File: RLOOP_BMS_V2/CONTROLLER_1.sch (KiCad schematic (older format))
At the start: 21 parts

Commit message: Bug Fixes
A few fixes and cleanup to make the ERC happy.
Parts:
- removed C? (x3): 100 nF / 50V/ 10% / SMD 0603, symbol C
- removed C?: 100n / 50V / 10% / SMD 0603, symbol C
- removed C? (x2): 100nF / 50V / 10% / SMD 0603, symbol C
- removed C? (x2): 10uF / 25V / 20% / SMD 1206, symbol C
- removed IC?: ATA6870N-PLQW-1, symbol ATA6870N-PLQW-1
- removed R?: 121K / 0.1W / 1% / SMD 0603, symbol R
- removed R? (x2): 10K / .1 W / 1% / SMD 0603, symbol R
- removed R?: 10, symbol R
- removed R?: 100k, symbol R
- removed TH? (x2): NTCS0603E3103JLT, symbol Thermistor_NTC
- added C16, C17: 10uF / 25V / 20% / SMD 1206, symbol C
- added C18, C20: 100nF / 50V / 10% / SMD 0603, symbol C
- added C19: 100n / 50V / 10% / SMD 0603, symbol C
- added C21, C22, C24: 100 nF / 50V/ 10% / SMD 0603, symbol C
- added IC4: ATA6870N-PLQW-1, symbol ATA6870N-PLQW-1
- added R12: 10, symbol R
- added R13: 121K / 0.1W / 1% / SMD 0603, symbol R
- added R14, R15: 10K / .1 W / 1% / SMD 0603, symbol R
- added TH3, TH4: NTCS0603E3103JLT, symbol Thermistor_NTC
- gave numbers to parts that had none: 5
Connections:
- net labels added: VDDHVP
- net labels removed: Thermal_Pad_3, ~PD_OUT
- wire segments 89 -> 86
- no-connect marks 0 -> 3
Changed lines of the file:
@@
 VDDHVM
 $Comp
-L ATA6870N-PLQW-1 IC?
-U 1 1 591D6F2A
+L ATA6870N-PLQW-1 IC4
+U 1 1 5917E38B
 P 5600 3400
-F 0 "IC?" H 6300 5200 60  0000 C CNN
+F 0 "IC4" H 6300 5200 60  0000 C CNN
 F 1 "ATA6870N-PLQW-1" H 6650 5100 60  0000 C CNN
 F 2 "" H 5550 3400 60  0001 C CNN
@@
 	-1   0    0    -1
 $EndComp
-Text HLabel 4100 2300 0    60   Output ~ 0
-~PD_OUT
 Text HLabel 2250 6900 0    60   Input ~ 0
 VDDHV
@@
 GND_1
 $Comp
-L C C?
-U 1 1 59101A84
+L C C21
+U 1 1 5917E364
 P 8350 1950
-F 0 "C?" H 8100 1950 50  0000 L CNN
+F 0 "C21" H 8100 1950 50  0000 L CNN
 F 1 "100 nF / 50V/ 10% / SMD 0603" H 8500 1950 50  0000 L CNN
 F 2 "" H 8388 1800 50  0001 C CNN
@@
 $EndComp
 $Comp
-L C C?
-U 1 1 59101A9B
+L C C22
+U 1 1 5917E366
 P 8350 2250
-F 0 "C?" H 8100 2250 50  0000 L CNN
+F 0 "C22" H 8100 2250 50  0000 L CNN
 F 1 "100 nF / 50V/ 10% / SMD 0603" H 8500 2250 50  0000 L CNN
 F 2 "" H 8388 2100 50  0001 C CNN
@@
 $EndComp
 $Comp
-L C C?
+L C C23
 U 1 1 59101AC2
 P 8350 2550
-F 0 "C?" H 8100 2550 50  0000 L CNN
+F 0 "C23" H 8100 2550 50  0000 L CNN
 F 1 "100 nF / 50V/ 10% / SMD 0603" H 8500 2550 50  0000 L CNN
 F 2 "" H 8388 2400 50  0001 C CNN
@@
 $EndComp
 $Comp
-L C C?
-U 1 1 59101ADD
+L C C24
+U 1 1 5917E36A
 P 8350 2850
-F 0 "C?" H 8100 2850 50  0000 L CNN
+F 0 "C24" H 8100 2850 50  0000 L CNN
 F 1 "100 nF / 50V/ 10% / SMD 0603" H 8500 2850 50  0000 L CNN
 F 2 "" H 8388 2700 50  0001 C CNN
@@
 $EndComp
 $Comp
-L C C?
+L C C25
 U 1 1 59101B02
 P 8350 3150
-F 0 "C?" H 8100 3150 50  0000 L CNN
+F 0 "C25" H 8100 3150 50  0000 L CNN
 F 1 "100 nF / 50V/ 10% / SMD 0603" H 8500 3150 50  0000 L CNN
 F 2 "" H 8388 3000 50  0001 C CNN
@@
 $EndComp
 $Comp
-L C C?
+L C C26
 U 1 1 59101B2D
 P 8350 3450
-F 0 "C?" H 8100 3450 50  0000 L CNN
+F 0 "C26" H 8100 3450 50  0000 L CNN
 F 1 "100 nF / 50V/ 10% / SMD 0603" H 8500 3450 50  0000 L CNN
 F 2 "" H 8388 3300 50  0001 C CNN
@@
 $EndComp
 $Comp
-L R R?
-U 1 1 59102664
+L R R13
+U 1 1 5917E371
 P 6900 4350
-F 0 "R?" V 6980 4350 50  0000 C CNN
+F 0 "R13" V 6980 4350 50  0000 C CNN
 F 1 "121K / 0.1W / 1% / SMD 0603" V 7050 4850 50  0000 C CNN
 F 2 "" V 6830 4350 50  0001 C CNN
@@
 GND_1
 $Comp
-L R R?
-U 1 1 591040ED
+L R R15
+U 1 1 5917E372
 P 9950 4050
-F 0 "R?" V 10030 4050 50  0000 C CNN
+F 0 "R15" V 10030 4050 50  0000 C CNN
 F 1 "10K / .1 W / 1% / SMD 0603" H 9300 4050 50  0000 C CNN
 F 2 "" V 9880 4050 50  0001 C CNN
@@
 $EndComp
 $Comp
-L Thermistor_NTC TH?
-U 1 1 59104176
+L Thermistor_NTC TH4
+U 1 1 5917E374
 P 9950 4550
-F 0 "TH?" V 9775 4550 50  0000 C CNN
+F 0 "TH4" V 9775 4550 50  0000 C CNN
 F 1 "NTCS0603E3103JLT" H 10450 4550 50  0000 C CNN
 F 2 "" H 9950 4600 50  0001 C CNN
@@
 $EndComp
 $Comp
-L Thermistor_NTC TH?
-U 1 1 5910419D
+L Thermistor_NTC TH3
+U 1 1 5917E377
 P 9000 4550
-F 0 "TH?" V 8825 4550 50  0000 C CNN
+F 0 "TH3" V 8825 4550 50  0000 C CNN
 F 1 "NTCS0603E3103JLT" H 9000 4350 50  0000 C CNN
 F 2 "" H 9000 4600 50  0001 C CNN
@@
 $EndComp
 $Comp
-L R R?
-U 1 1 591041CA
+L R R14
+U 1 1 5917E378
 P 9000 4050
-F 0 "R?" V 9080 4050 50  0000 C CNN
+F 0 "R14" V 9080 4050 50  0000 C CNN
 F 1 "10K / .1 W / 1% / SMD 0603" H 9200 4200 50  0000 C CNN
 F 2 "" V 8930 4050 50  0001 C CNN
@@
 GND_1
 $Comp
-L C C?
+L C C28
 U 1 1 59105042
 P 9550 4550
-F 0 "C?" H 9575 4650 50  0000 L CNN
+F 0 "C28" H 9575 4650 50  0000 L CNN
 F 1 "100n" H 9250 4550 50  0000 L CNN
 F 2 "" H 9588 4400 50  0001 C CNN
@@
 $EndComp
 $Comp
-L C C?
+L C C27
 U 1 1 591051E7
 P 8450 4550
-F 0 "C?" H 8475 4650 50  0000 L CNN
+F 0 "C27" H 8475 4650 50  0000 L CNN
 F 1 "100n" H 8200 4450 50  0000 L CNN
 F 2 "" H 8488 4400 50  0001 C CNN
@@
 $EndComp
 $Comp
-L R R?
-U 1 1 5910D275
+L R R12
+U 1 1 5917E381
 P 2650 6900
-F 0 "R?" V 2730 6900 50  0000 C CNN
+F 0 "R12" V 2730 6900 50  0000 C CNN
 F 1 "10" V 2650 6900 50  0000 C CNN
 F 2 "" V 2580 6900 50  0001 C CNN
@@
 $EndComp
 $Comp
-L C C?
-U 1 1 5910D5BF
+L C C20
+U 1 1 5917E382
 P 6750 2000
-F 0 "C?" H 6775 2100 50  0000 L CNN
+F 0 "C20" H 6775 2100 50  0000 L CNN
 F 1 "100nF / 50V / 10% / SMD 0603" H 5400 2150 50  0000 L CNN
 F 2 "" H 6788 1850 50  0001 C CNN
@@
 $EndComp
 $Comp
-L C C?
-U 1 1 5910D5FC
+L C C17
+U 1 1 5917E385
 P 3200 7150
-F 0 "C?" H 3225 7250 50  0000 L CNN
+F 0 "C17" H 3225 7250 50  0000 L CNN
 F 1 "10uF / 25V / 20% / SMD 1206" H 1750 7150 50  0000 L CNN
 F 2 "" H 3238 7000 50  0001 C CNN
@@
 $EndComp
 $Comp
-L R R?
-U 1 1 591108C7
-P 4200 4850
-F 0 "R?" V 4100 4850 50  0000 C CNN
-F 1 "100k" V 4200 4850 50  0000 C CNN
-F 2 "" V 4130 4850 50  0001 C CNN
-F 3 "" H 4200 4850 50  0001 C CNN
-	1    4200 4850
-	0    1    1    0
-$EndComp
-$Comp
-L C C?
-U 1 1 5910B934
+L C C19
+U 1 1 5917E37E
 P 5450 1700
-F 0 "C?" H 5475 1800 50  0000 L CNN
+F 0 "C19" H 5475 1800 50  0000 L CNN
 F 1 "100n / 50V / 10% / SMD 0603" H 5250 1900 50  0000 L CNN
 F 2 "" H 5488 1550 50  0001 C CNN
@@
 Text GLabel 6850 2200 2    60   Input ~ 0
 VDDHV_1
-Text GLabel 4100 2550 0    60   Input ~ 0
-VDDHV_1
-Text Label 5200 6000 1    60   ~ 0
-Thermal_Pad_3
 Text GLabel 6750 1750 1    60   Input ~ 0
 GND_1
 $Comp
-L C C?
-U 1 1 59119745
+L C C18
+U 1 1 5917E386
 P 3250 2800
-F 0 "C?" H 3275 2900 50  0000 L CNN
+F 0 "C18" H 3275 2900 50  0000 L CNN
 F 1 "100nF / 50V / 10% / SMD 0603" H 3275 2700 50  0000 L CNN
 F 2 "" H 3288 2650 50  0001 C CNN
@@
 Wire Wire Line
 	4100 2200 4450 2200
-Wire Wire Line
-	4450 2300 4100 2300
 Wire Wire Line
 	4100 3850 4450 3850
@@
 Connection ~ 5850 5450
 Wire Wire Line
-	4450 4850 4350 4850
-Wire Wire Line
-	3900 4850 4050 4850
-Wire Wire Line
-	3550 4950 4450 4950
-Wire Wire Line
 	4300 1850 5650 1850
 Connection ~ 5450 1850
@@
 	4100 2550 4450 2550
 Wire Wire Line
-	5250 5300 5250 6000
-Wire Wire Line
 	6650 3800 9950 3800
 Wire Wire Line
@@
 Connection ~ 9000 5100
 Wire Wire Line
-	5250 6000 5200 6000
-Wire Wire Line
 	6750 2150 6750 2200
 Connection ~ 6750 2200
@@
 Connection ~ 3250 2650
 $Comp
-L C C?
-U 1 1 5911BED4
+L C C16
+U 1 1 5917E388
 P 2700 2800
-F 0 "C?" H 2725 2900 50  0000 L CNN
+F 0 "C16" H 2725 2900 50  0000 L CNN
 F 1 "10uF / 25V / 20% / SMD 1206" H 1300 2800 50  0000 L CNN
 F 2 "" H 2738 2650 50  0001 C CNN
@@
 Wire Wire Line
 	4450 3650 4100 3650
-Text GLabel 3550 4950 0    60   Input ~ 0
-GND_1
-Wire Wire Line
-	3900 4750 3900 4950
-Connection ~ 3900 4950
-Wire Wire Line
-	4450 4750 3900 4750
-Connection ~ 3900 4850
 Wire Wire Line
 	4300 4550 4450 4550
 Connection ~ 4300 2850
+Text HLabel 4100 2550 0    60   Input ~ 0
+VDDHVP
+NoConn ~ 4450 4950
+NoConn ~ 4450 4850
+NoConn ~ 4450 4750
+Text GLabel 4100 2300 0    60   Input ~ 0
+GND_1
+Wire Wire Line
+	4100 2300 4450 2300
+Text GLabel 12250 2950 0    60   Input ~ 0
+GND_1
+Text GLabel 12250 3200 0    60   Input ~ 0
+VDDHV_1
+$Comp
+L PWR_FLAG #FLG03
+U 1 1 591903A2
+P 12500 2650
+F 0 "#FLG03" H 12500 2725 50  0001 C CNN
+F 1 "PWR_FLAG" H 12500 2800 50  0000 C CNN
+F 2 "" H 12500 2650 50  0001 C CNN
+F 3 "" H 12500 2650 50  0001 C CNN
+	1    12500 2650
+	1    0    0    -1
+$EndComp
+$Comp
+L PWR_FLAG #FLG04
+U 1 1 591903DE
+P 13000 2650
+F 0 "#FLG04" H 13000 2725 50  0001 C CNN
+F 1 "PWR_FLAG" H 13000 2800 50  0000 C CNN
+F 2 "" H 13000 2650 50  0001 C CNN
+F 3 "" H 13000 2650 50  0001 C CNN
+	1    13000 2650
+	1    0    0    -1
+$EndComp
+Wire Wire Line
+	12500 2650 12500 2950
+Wire Wire Line
+	12500 2950 12250 2950
+Wire Wire Line
+	12250 3200 13000 3200
+Wire Wire Line
+	13000 3200 13000 2650
 $EndSCHEMATC

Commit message: Footprint work
starting to assign footprints to parts
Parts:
- C16, C17: footprint (none) -> Capacitors_SMD:C_1206
- C18, C19, C20, C21, C22, C23, C24, C25, C26, C27, C28: footprint (none) -> Capacitors_SMD:C_0603
- R12, R13, R14, R15: footprint (none) -> Resistors_SMD:R_0603
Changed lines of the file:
@@
 F 0 "C21" H 8100 1950 50  0000 L CNN
 F 1 "100 nF / 50V/ 10% / SMD 0603" H 8500 1950 50  0000 L CNN
-F 2 "" H 8388 1800 50  0001 C CNN
+F 2 "Capacitors_SMD:C_0603" H 8388 1800 50  0001 C CNN
 F 3 "" H 8350 1950 50  0001 C CNN
 	1    8350 1950
@@
 F 0 "C22" H 8100 2250 50  0000 L CNN
 F 1 "100 nF / 50V/ 10% / SMD 0603" H 8500 2250 50  0000 L CNN
-F 2 "" H 8388 2100 50  0001 C CNN
+F 2 "Capacitors_SMD:C_0603" H 8388 2100 50  0001 C CNN
 F 3 "" H 8350 2250 50  0001 C CNN
 	1    8350 2250
@@
 F 0 "C23" H 8100 2550 50  0000 L CNN
 F 1 "100 nF / 50V/ 10% / SMD 0603" H 8500 2550 50  0000 L CNN
-F 2 "" H 8388 2400 50  0001 C CNN
+F 2 "Capacitors_SMD:C_0603" H 8388 2400 50  0001 C CNN
 F 3 "" H 8350 2550 50  0001 C CNN
 	1    8350 2550
@@
 F 0 "C24" H 8100 2850 50  0000 L CNN
 F 1 "100 nF / 50V/ 10% / SMD 0603" H 8500 2850 50  0000 L CNN
-F 2 "" H 8388 2700 50  0001 C CNN
+F 2 "Capacitors_SMD:C_0603" H 8388 2700 50  0001 C CNN
 F 3 "" H 8350 2850 50  0001 C CNN
 	1    8350 2850
@@
 F 0 "C25" H 8100 3150 50  0000 L CNN
 F 1 "100 nF / 50V/ 10% / SMD 0603" H 8500 3150 50  0000 L CNN
-F 2 "" H 8388 3000 50  0001 C CNN
+F 2 "Capacitors_SMD:C_0603" H 8388 3000 50  0001 C CNN
 F 3 "" H 8350 3150 50  0001 C CNN
 	1    8350 3150
@@
 F 0 "C26" H 8100 3450 50  0000 L CNN
 F 1 "100 nF / 50V/ 10% / SMD 0603" H 8500 3450 50  0000 L CNN
-F 2 "" H 8388 3300 50  0001 C CNN
+F 2 "Capacitors_SMD:C_0603" H 8388 3300 50  0001 C CNN
 F 3 "" H 8350 3450 50  0001 C CNN
 	1    8350 3450
@@
 F 0 "R13" V 6980 4350 50  0000 C CNN
 F 1 "121K / 0.1W / 1% / SMD 0603" V 7050 4850 50  0000 C CNN
-F 2 "" V 6830 4350 50  0001 C CNN
+F 2 "Resistors_SMD:R_0603" V 6830 4350 50  0001 C CNN
 F 3 "" H 6900 4350 50  0001 C CNN
 	1    6900 4350
@@
 F 0 "R15" V 10030 4050 50  0000 C CNN
 F 1 "10K / .1 W / 1% / SMD 0603" H 9300 4050 50  0000 C CNN
-F 2 "" V 9880 4050 50  0001 C CNN
+F 2 "Resistors_SMD:R_0603" V 9880 4050 50  0001 C CNN
 F 3 "" H 9950 4050 50  0001 C CNN
 	1    9950 4050
@@
 F 0 "R14" V 9080 4050 50  0000 C CNN
 F 1 "10K / .1 W / 1% / SMD 0603" H 9200 4200 50  0000 C CNN
-F 2 "" V 8930 4050 50  0001 C CNN
+F 2 "Resistors_SMD:R_0603" V 8930 4050 50  0001 C CNN
 F 3 "" H 9000 4050 50  0001 C CNN
 	1    9000 4050
@@
 F 0 "C28" H 9575 4650 50  0000 L CNN
 F 1 "100n" H 9250 4550 50  0000 L CNN
-F 2 "" H 9588 4400 50  0001 C CNN
+F 2 "Capacitors_SMD:C_0603" H 9588 4400 50  0001 C CNN
 F 3 "" H 9550 4550 50  0001 C CNN
 	1    9550 4550
@@
 F 0 "C27" H 8475 4650 50  0000 L CNN
 F 1 "100n" H 8200 4450 50  0000 L CNN
-F 2 "" H 8488 4400 50  0001 C CNN
+F 2 "Capacitors_SMD:C_0603" H 8488 4400 50  0001 C CNN
 F 3 "" H 8450 4550 50  0001 C CNN
 	1    8450 4550
@@
 F 0 "R12" V 2730 6900 50  0000 C CNN
 F 1 "10" V 2650 6900 50  0000 C CNN
-F 2 "" V 2580 6900 50  0001 C CNN
+F 2 "Resistors_SMD:R_0603" V 2580 6900 50  0001 C CNN
 F 3 "" H 2650 6900 50  0001 C CNN
 	1    2650 6900
@@
 F 0 "C20" H 6775 2100 50  0000 L CNN
 F 1 "100nF / 50V / 10% / SMD 0603" H 5400 2150 50  0000 L CNN
-F 2 "" H 6788 1850 50  0001 C CNN
+F 2 "Capacitors_SMD:C_0603" H 6788 1850 50  0001 C CNN
 F 3 "" H 6750 2000 50  0001 C CNN
 	1    6750 2000
@@
 F 0 "C17" H 3225 7250 50  0000 L CNN
 F 1 "10uF / 25V / 20% / SMD 1206" H 1750 7150 50  0000 L CNN
-F 2 "" H 3238 7000 50  0001 C CNN
+F 2 "Capacitors_SMD:C_1206" H 3238 7000 50  0001 C CNN
 F 3 "" H 3200 7150 50  0001 C CNN
 	1    3200 7150
@@
 F 0 "C19" H 5475 1800 50  0000 L CNN
 F 1 "100n / 50V / 10% / SMD 0603" H 5250 1900 50  0000 L CNN
-F 2 "" H 5488 1550 50  0001 C CNN
+F 2 "Capacitors_SMD:C_0603" H 5488 1550 50  0001 C CNN
 F 3 "" H 5450 1700 50  0001 C CNN
 	1    5450 1700
@@
 F 0 "C18" H 3275 2900 50  0000 L CNN
 F 1 "100nF / 50V / 10% / SMD 0603" H 3275 2700 50  0000 L CNN
-F 2 "" H 3288 2650 50  0001 C CNN
+F 2 "Capacitors_SMD:C_0603" H 3288 2650 50  0001 C CNN
 F 3 "" H 3250 2800 50  0001 C CNN
 	1    3250 2800
@@
 F 0 "C16" H 2725 2900 50  0000 L CNN
 F 1 "10uF / 25V / 20% / SMD 1206" H 1300 2800 50  0000 L CNN
-F 2 "" H 2738 2650 50  0001 C CNN
+F 2 "Capacitors_SMD:C_1206" H 2738 2650 50  0001 C CNN
 F 3 "" H 2700 2800 50  0001 C CNN
 	1    2700 2800

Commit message: footprint and layout work WIP
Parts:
- IC4: footprint (none) -> rLoop_Footprints:ATA6870-QFN48
- TH3, TH4: footprint (none) -> Resistors_SMD:R_0603
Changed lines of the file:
@@
 F 0 "IC4" H 6300 5200 60  0000 C CNN
 F 1 "ATA6870N-PLQW-1" H 6650 5100 60  0000 C CNN
-F 2 "" H 5550 3400 60  0001 C CNN
+F 2 "rLoop_Footprints:ATA6870-QFN48" H 5550 3400 60  0001 C CNN
 F 3 "" H 5550 3400 60  0001 C CNN
 	1    5600 3400
@@
 F 0 "TH4" V 9775 4550 50  0000 C CNN
 F 1 "NTCS0603E3103JLT" H 10450 4550 50  0000 C CNN
-F 2 "" H 9950 4600 50  0001 C CNN
+F 2 "Resistors_SMD:R_0603" H 9950 4600 50  0001 C CNN
 F 3 "" H 9950 4600 50  0001 C CNN
 	1    9950 4550
@@
 F 0 "TH3" V 8825 4550 50  0000 C CNN
 F 1 "NTCS0603E3103JLT" H 9000 4350 50  0000 C CNN
-F 2 "" H 9000 4600 50  0001 C CNN
+F 2 "Resistors_SMD:R_0603" H 9000 4600 50  0001 C CNN
 F 3 "" H 9000 4600 50  0001 C CNN
 	1    9000 4550

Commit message: WIP
See if it's even possible
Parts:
- removed C16, C17: 10uF / 25V / 20% / SMD 1206, Capacitors_SMD:C_1206, symbol C
- removed C18, C20: 100nF / 50V / 10% / SMD 0603, Capacitors_SMD:C_0603, symbol C
- removed C19: 100n / 50V / 10% / SMD 0603, Capacitors_SMD:C_0603, symbol C
- removed C27, C28: 100n, Capacitors_SMD:C_0603, symbol C
- removed IC4: ATA6870N-PLQW-1, rLoop_Footprints:ATA6870-QFN48, symbol ATA6870N-PLQW-1
- removed R12: 10, Resistors_SMD:R_0603, symbol R
- removed R13: 121K / 0.1W / 1% / SMD 0603, Resistors_SMD:R_0603, symbol R
- removed R14, R15: 10K / .1 W / 1% / SMD 0603, Resistors_SMD:R_0603, symbol R
- removed TH3, TH4: NTCS0603E3103JLT, Resistors_SMD:R_0603, symbol Thermistor_NTC
- added 1M1: R, symbol R
- added C5: 10 uF / 50V/ 10% / SMD 0603, symbol C
- added R2, R3, R4: 1k, symbol R
- added U3: bq76PL536A_HTQFP, symbol bq76PL536A_HTQFP
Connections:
- net labels added: 5V_1, CS_H, CS_N, SCLK_H, SCLK_N, SDI_H, SDI_N, SDO_H, SDO_N
- net labels removed: CLK_IN, CLK_OUT, IRQ_IN, IRQ_OUT, SPI_MISO_LWR, SPI_MISO_UP, SPI_MOSI_LWR, SPI_MOSI_UP, SPI_NCS_LWR, SPI_NCS_UP, SPI_SCK_LWR, SPI_SCK_UP, VDDHVM, VDDHVP, ~PD_IN
- wire segments 86 -> 76
- no-connect marks 3 -> 16
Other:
- moved on the sheet: C21, C22, C23, C24, C25, C26

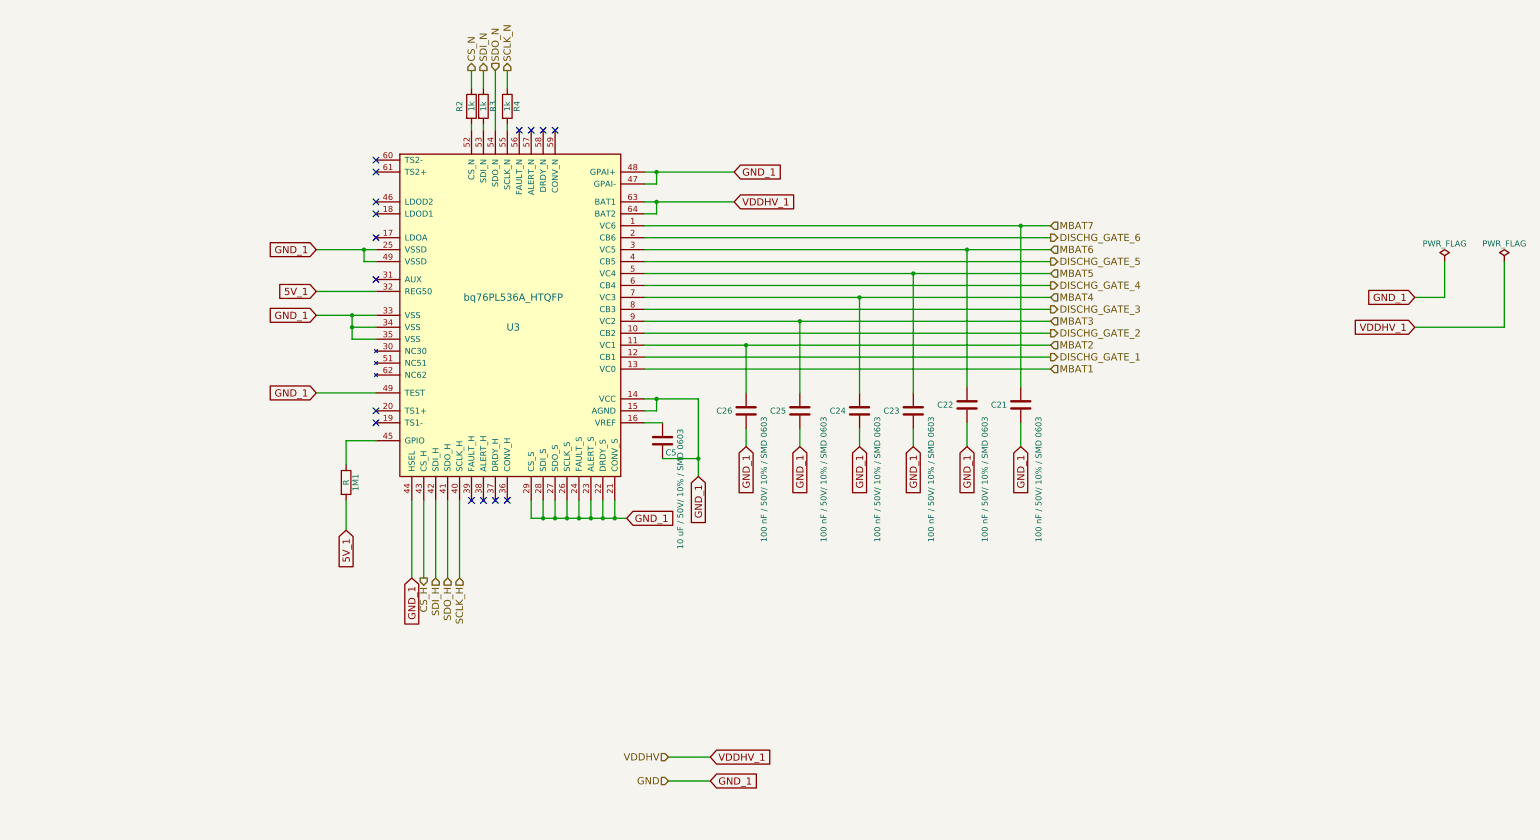
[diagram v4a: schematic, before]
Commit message: Ti BMS WIP
Getting there. Need to add temp sensors, fan control, and an LDO for the
SPI ISO supply.
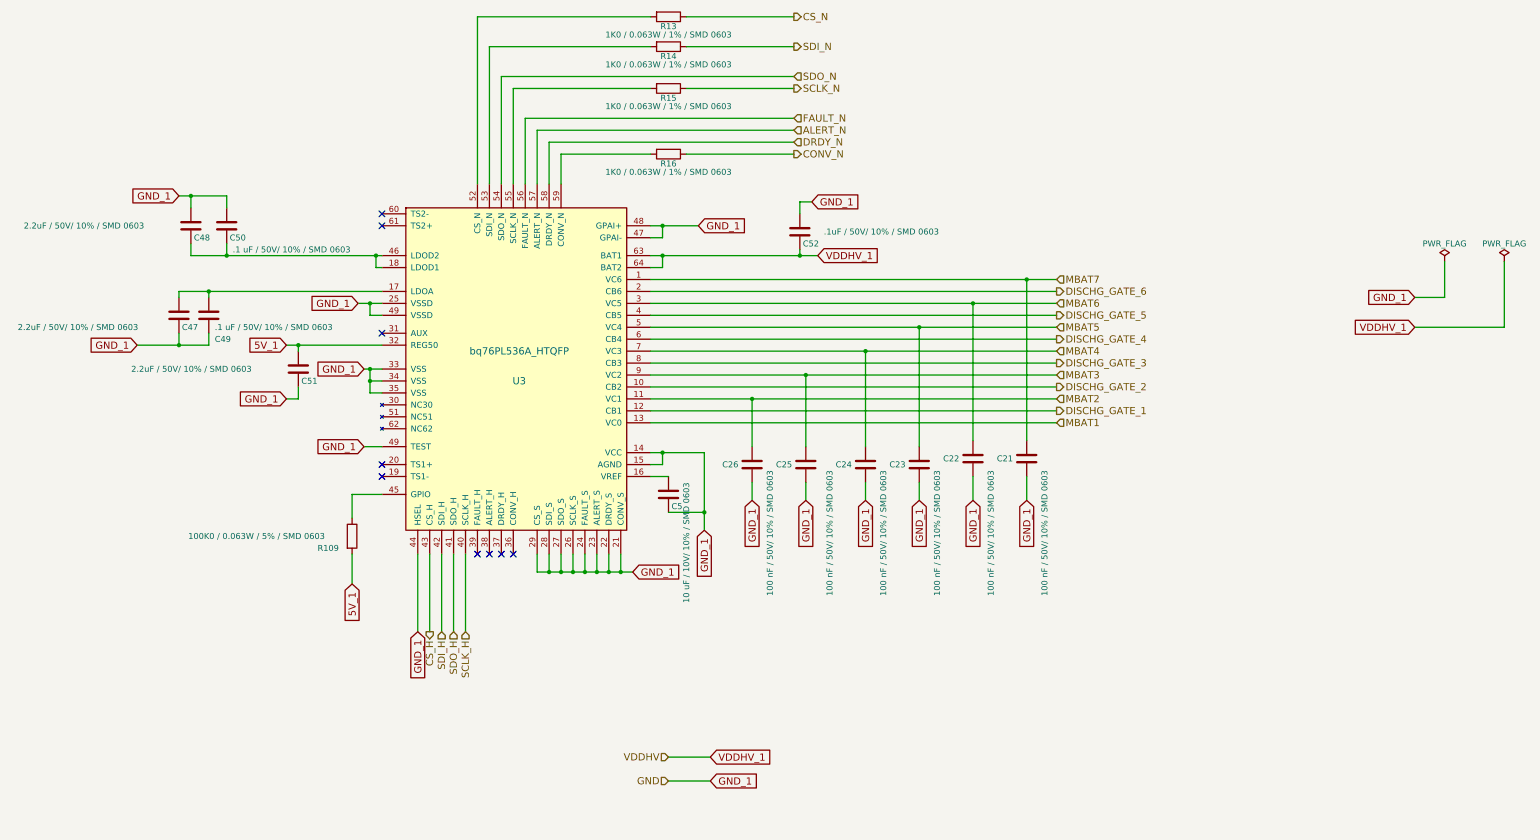
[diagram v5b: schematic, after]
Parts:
- removed R2, R3, R4: 1k, symbol R
- added C47, C48, C51: 2.2uF / 50V/ 10% / SMD 0603, Capacitors_SMD:C_0603, symbol C
- added C49, C50: .1 uF / 50V/ 10% / SMD 0603, Capacitors_SMD:C_0603, symbol C
- added C52: .1uF / 50V/ 10% / SMD 0603, Capacitors_SMD:C_0603, symbol C
- added R13, R14, R15, R16: 1K0 / 0.063W / 1% / SMD 0603, Resistors_SMD:R_0603, symbol R
- C5: value 10 uF / 50V/ 10% / SMD 0603 -> 10 uF / 10V/ 10% / SMD 0603; footprint (none) -> Capacitors_SMD:C_0603
- R109: renamed from 1M1; value R -> 100K0 / 0.063W / 5% / SMD 0603; footprint (none) -> Resistors_SMD:R_0603
- U3: footprint (none) -> rLoop_Footprints:bq76pl536a
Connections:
- net 5V_1: now also C51.2
- net CS_N: now also R13.1
- net GND_1: now also C47.1, C48.2, C49.1, C50.2, C51.1, C52.2
- net SCLK_N: now also R15.1
- net SDI_N: now also R14.1
- net VDDHV_1: now also C52.1
- net at U3.17 (LDOA): now also C47.2, C49.2
- net at U3.18 (LDOD1): now also U3.46 (LDOD2), C48.1, C50.1
- net at U3.52 (CS_N): now also R13.2
- net at U3.53 (SDI_N): now also R14.2
- net at U3.55 (SCLK_N): now also R15.2
- net FAULT_N: now reaches U3.56 (FAULT_N)
- net ALERT_N: now reaches U3.57 (ALERT_N)
- net DRDY_N: now reaches U3.58 (DRDY_N)
- net at U3.59 (CONV_N): now also R16.2
- new net CONV_N: R16.1
- no-connect marks 16 -> 9
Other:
- moved on the sheet: C21, C22, C23, C24, C25, C26, C5, R109, U3

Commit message: More WIP on BMS v2.5
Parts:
- added C? (x2): .047 uF / 50V/ 10% / SMD 0603, Capacitors_SMD:C_0603, symbol C
- added R? (x2): 1.82k / 0.063W / 1% / SMD0603, symbol R
- added R? (x2): 1.47k / 0.063W / 1% / SMD0603, symbol R
- added TH? (x2): 10k / 1% / 3454K / SMD0603, symbol Thermistor_NTC
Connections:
- net 5V_1: now also C?.1, C?.2, TH?.1, TH?.2
- net at U3.19 (TS1-): now also R?.1
- net at U3.20 (TS1+): now also C?.2, R?.1, R?.2
- net at U3.60 (TS2-): now also R?.1
- net at U3.61 (TS2+): now also C?.1, R?.1, R?.2
- new net: R?.2, TH?.2
- new net: R?.2, TH?.1
- no-connect marks 9 -> 5
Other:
- moved on the sheet: C21, C22, C23, C24, C25, C26, C47, C48, C49, C5, C50, C51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
